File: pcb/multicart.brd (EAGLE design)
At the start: 55.5 x 86.4 mm, 14 parts, among them IC1 74HCT373N, IC2 M27C4001B, Q1 BS170

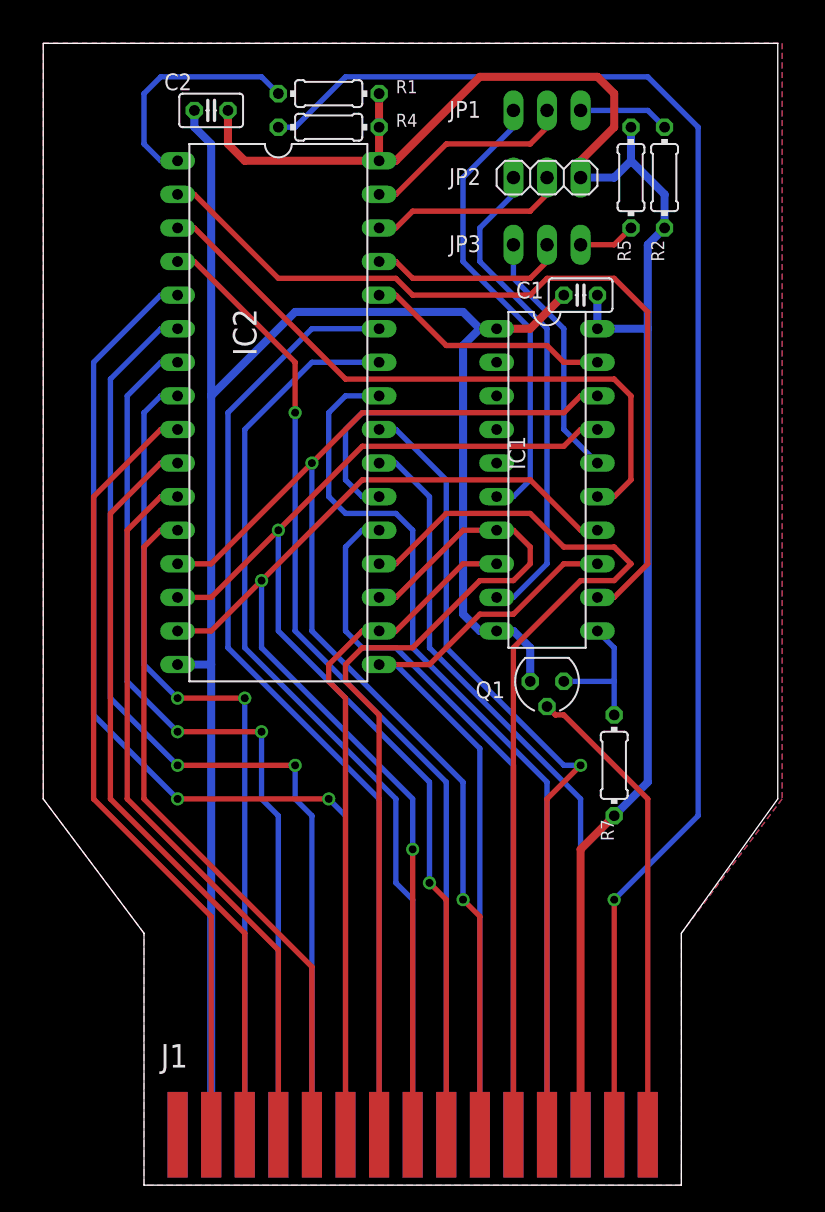
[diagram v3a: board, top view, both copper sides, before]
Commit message: Modified the design to support both 8k and 16k standard games.
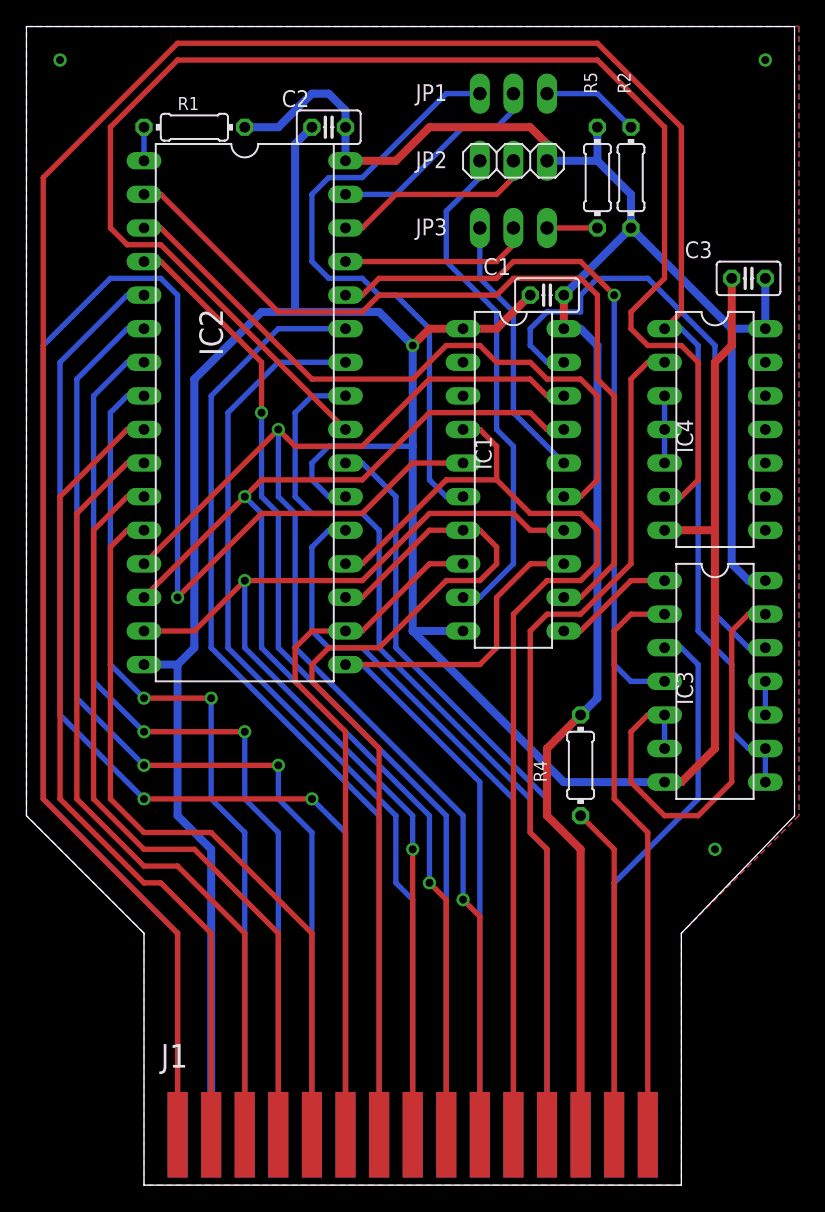
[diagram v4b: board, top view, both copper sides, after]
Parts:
- removed Q1: BS170, transistor-small-signal:SOT54E
- removed R7: 4k7, resistor:0204/7
- added C3: 100n, resistor:C025-025X050
- added IC3: 74HCT02N, 74xx-eu:DIL14
- added IC4: 74HCT00N, 74xx-eu:DIL14
- moved R4 51.9 mm to (47.0, 29.2), turned to 270 degrees
- moved R1 10.5 mm to (17.8, 77.5)
- moved C2 8.98 mm to (27.9, 77.5)
- moved JP1 2.84 mm to (41.9, 80.0)
- moved JP2 2.84 mm to (41.9, 74.9)
- moved JP3 2.84 mm to (41.9, 69.8)
- moved IC1 2.54 mm to (41.9, 50.8)
- moved R2 2.54 mm to (50.8, 73.7)
- moved C1 2.54 mm to (44.5, 64.8)
- moved IC2 2.54 mm to (21.6, 55.9)
- moved R5 2.54 mm to (48.3, 73.7)
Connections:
- new net N$14: IC4.3, IC4.4, IC4.5
- new net N$18: IC4.2, J1.12
- new net N$19: IC3.8, IC3.9, IC4.1, J1.1
- new net N$20: IC3.3, J1.R
- new net N$21: IC2.28, IC3.4
- new net N$22: IC1.5, J1.A
- new net N$23: IC3.13, IC3.5, IC3.6
- new net N$27: IC2.24, IC4.6
- net D6: now also IC1.4
- net GND: now also C3.2, IC3.7, IC4.7; no longer Q1.S
- net N$1: now also IC3.12; no longer IC2.28
- net N$17: now also IC3.10, IC3.11; no longer IC2.24, J1.12
- net N$7: now also IC3.1; no longer Q1.D, R7.1
- net N$8: now also IC3.2; no longer Q1.G
- net VCC: now also C3.1, IC3.14, IC4.14; no longer R7.2
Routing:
- net N$19: track 0.00 -> 186.4 mm
- net N$22: track 0.00 -> 125.3 mm, vias 0 -> 1
- net N$27: track 0.00 -> 112.2 mm
- net N$13: track 113.7 -> 25.2 mm, vias 1 -> 0
- net N$18: track 0.00 -> 65.4 mm
- net N$17: track 62.2 -> 2.54 mm, vias 1 -> 0
- net GND: track 158.5 -> 213.6 mm, vias 0 -> 1
- net N$21: track 0.00 -> 54.7 mm, vias 0 -> 1
- net N$20: track 0.00 -> 41.3 mm
- net N$23: track 0.00 -> 33.6 mm
- net N$1: track 18.6 -> 47.9 mm
- net VCC: track 138.5 -> 156.7 mm
- net N$9: track 18.1 -> 2.54 mm
- net N$6: track 34.7 -> 46.4 mm
- net D6: track 70.6 -> 78.7 mm
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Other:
- board size 55.5 x 86.4 mm -> 58.1 x 87.6 mm

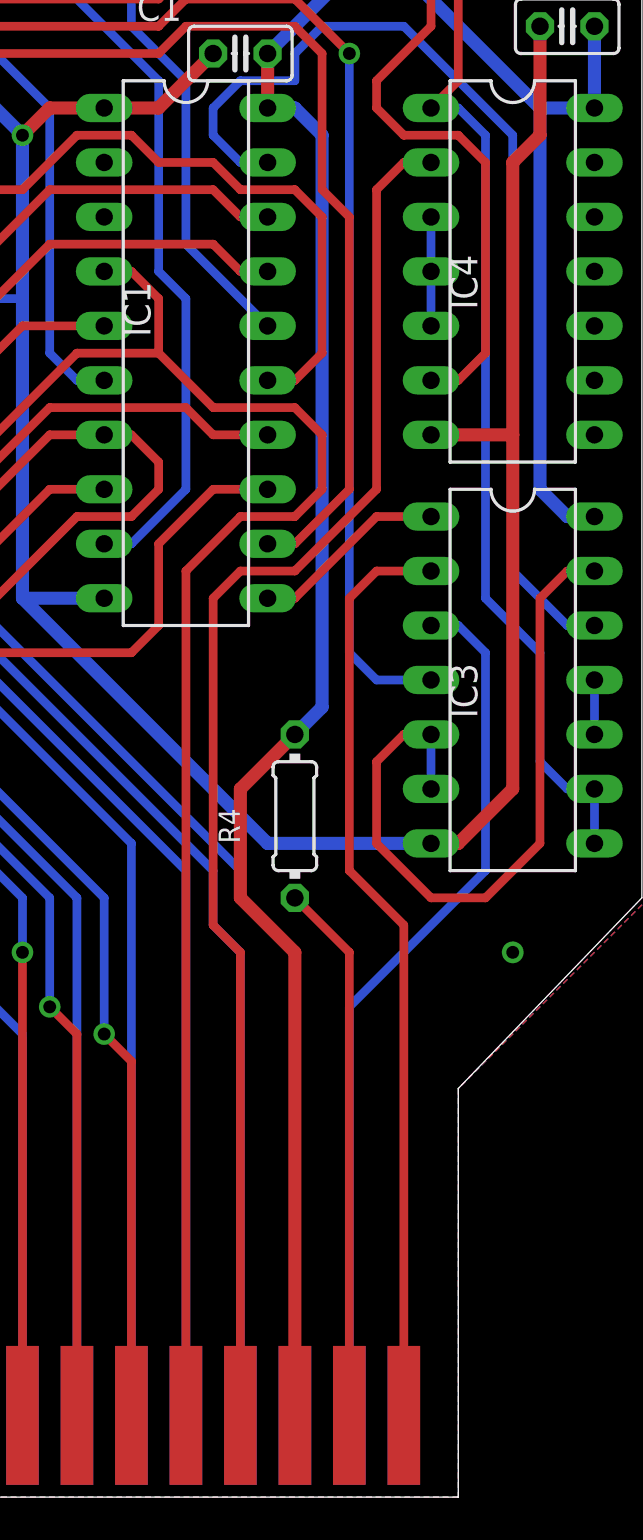
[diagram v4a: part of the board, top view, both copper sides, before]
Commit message: Removed the RD5 line resistor.
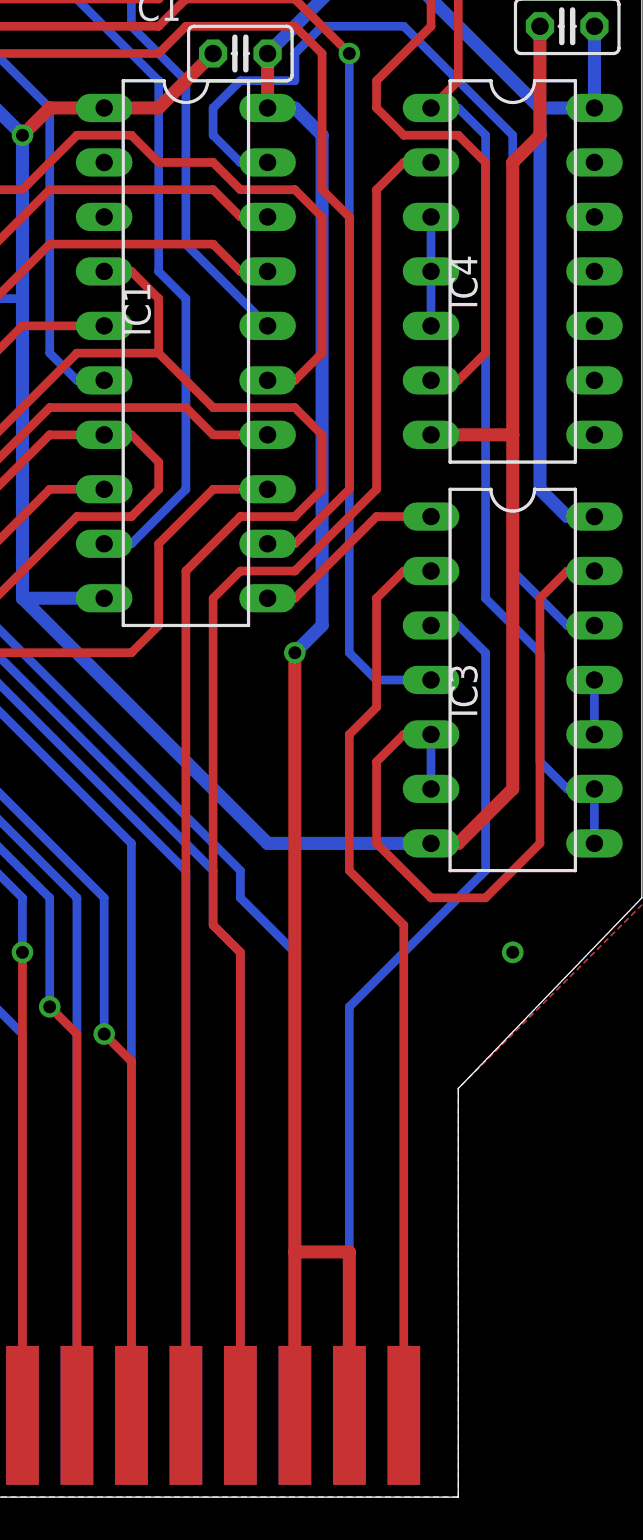
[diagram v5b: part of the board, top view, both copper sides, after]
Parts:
- removed R4: 4k7, resistor:0204/7
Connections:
- removed net N$13: J1.14, R4.2
- net VCC: now also J1.14; no longer R4.1
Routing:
- net N$13: track 25.2 -> 0.00 mm
- net VCC: track 156.7 -> 164.7 mm, vias 0 -> 1
- net N$8: track 43.5 -> 42.7 mm
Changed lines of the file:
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@@
 <attribute name="VALUE" x="50.6476" y="73.3044" size="0.9906" layer="27" ratio="10" rot="R90"/>
-</element>
-<element name="R4" library="resistor" package="0204/7" value="4k7" x="46.99" y="29.21" smashed="yes" rot="R270">
-<attribute name="NAME" x="44.4246" y="27.94" size="0.9906" layer="25" ratio="10" rot="R90"/>
-<attribute name="VALUE" x="46.2026" y="28.8544" size="0.9906" layer="27" ratio="10" rot="R90"/>
 </element>
 <element name="R5" library="resistor" package="0204/7" value="4k7" x="48.26" y="73.66" smashed="yes" rot="R90">
@@
 <contactref element="R2" pad="2"/>
 <contactref element="R5" pad="2"/>
-<wire x1="46.99" y1="22.86" x2="46.99" y2="1.27" width="0.6096" layer="1"/>
+<wire x1="46.99" y1="36.83" x2="46.99" y2="8.89" width="0.6096" layer="1"/>
+<wire x1="46.99" y1="8.89" x2="46.99" y2="1.27" width="0.6096" layer="1"/>
 <wire x1="50.8" y1="69.85" x2="50.8" y2="72.39" width="0.6096" layer="16"/>
 <wire x1="48.26" y1="77.47" x2="48.26" y2="74.93" width="0.6096" layer="16"/>
@@
 <contactref element="IC3" pad="14"/>
 <contactref element="IC4" pad="14"/>
-<contactref element="R4" pad="1"/>
-<wire x1="44.45" y1="30.48" x2="46.99" y2="33.02" width="0.6096" layer="1"/>
 <wire x1="60.96" y1="43.18" x2="59.69" y2="43.18" width="0.6096" layer="16"/>
 <wire x1="59.69" y1="43.18" x2="58.42" y2="44.45" width="0.6096" layer="16"/>
@@
 <wire x1="27.94" y1="80.01" x2="29.21" y2="78.74" width="0.6096" layer="16"/>
 <wire x1="29.21" y1="78.74" x2="29.21" y2="77.47" width="0.6096" layer="16"/>
-<wire x1="48.26" y1="34.29" x2="46.99" y2="33.02" width="0.6096" layer="16"/>
 <wire x1="58.42" y1="62.23" x2="50.8" y2="69.85" width="0.6096" layer="16"/>
 <wire x1="45.72" y1="64.77" x2="50.8" y2="69.85" width="0.6096" layer="16"/>
-<wire x1="46.99" y1="22.86" x2="44.45" y2="25.4" width="0.6096" layer="1"/>
-<wire x1="44.45" y1="25.4" x2="44.45" y2="30.48" width="0.6096" layer="1"/>
 <wire x1="29.21" y1="74.93" x2="33.02" y2="74.93" width="0.6096" layer="1"/>
 <wire x1="33.02" y1="74.93" x2="35.56" y2="77.47" width="0.6096" layer="1"/>
@@
 <wire x1="43.18" y1="77.47" x2="44.45" y2="76.2" width="0.6096" layer="1"/>
 <wire x1="44.45" y1="76.2" x2="44.45" y2="74.93" width="0.6096" layer="1"/>
-<wire x1="48.26" y1="34.29" x2="48.26" y2="60.96" width="0.6096" layer="16"/>
+<wire x1="45.72" y1="62.23" x2="45.72" y2="64.77" width="0.6096" layer="1"/>
+<contactref element="J1" pad="14"/>
+<wire x1="49.53" y1="1.27" x2="49.53" y2="8.89" width="0.6096" layer="1"/>
+<wire x1="49.53" y1="8.89" x2="46.99" y2="8.89" width="0.6096" layer="1"/>
+<via x="46.99" y="36.83" extent="1-16" drill="0.6" shape="octagon"/>
+<wire x1="46.99" y1="36.83" x2="48.26" y2="38.1" width="0.6096" layer="16"/>
+<wire x1="48.26" y1="38.1" x2="48.26" y2="60.96" width="0.6096" layer="16"/>
 <wire x1="48.26" y1="60.96" x2="46.99" y2="62.23" width="0.6096" layer="16"/>
 <wire x1="46.99" y1="62.23" x2="45.72" y2="62.23" width="0.6096" layer="16"/>
-<wire x1="45.72" y1="62.23" x2="45.72" y2="64.77" width="0.6096" layer="1"/>
 </signal>
 <signal name="GND">
@@
 <contactref element="J1" pad="15"/>
 <contactref element="IC3" pad="2"/>
-<wire x1="49.53" y1="39.37" x2="50.8" y2="40.64" width="0.4064" layer="1"/>
-<wire x1="50.8" y1="40.64" x2="53.34" y2="40.64" width="0.4064" layer="1"/>
 <wire x1="52.07" y1="1.27" x2="52.07" y2="24.13" width="0.4064" layer="1"/>
 <wire x1="52.07" y1="24.13" x2="49.53" y2="26.67" width="0.4064" layer="1"/>
-<wire x1="49.53" y1="26.67" x2="49.53" y2="39.37" width="0.4064" layer="1"/>
+<wire x1="53.34" y1="40.64" x2="52.07" y2="40.64" width="0.4064" layer="1"/>
+<wire x1="52.07" y1="40.64" x2="50.8" y2="39.37" width="0.4064" layer="1"/>
+<wire x1="50.8" y1="39.37" x2="50.8" y2="34.29" width="0.4064" layer="1"/>
+<wire x1="50.8" y1="34.29" x2="49.53" y2="33.02" width="0.4064" layer="1"/>
+<wire x1="49.53" y1="33.02" x2="49.53" y2="26.67" width="0.4064" layer="1"/>
 </signal>
 <signal name="N$21">
@@
 <wire x1="55.88" y1="26.67" x2="49.53" y2="20.32" width="0.4064" layer="16"/>
 </signal>
-<signal name="N$13">
-<contactref element="J1" pad="14"/>
-<contactref element="R4" pad="2"/>
-<wire x1="49.53" y1="1.27" x2="49.53" y2="22.86" width="0.4064" layer="1"/>
-<wire x1="49.53" y1="22.86" x2="46.99" y2="25.4" width="0.4064" layer="1"/>
-</signal>
 <signal name="N$17">

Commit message: Optimized the design a little.
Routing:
- net N$6: track 46.4 -> 34.6 mm
- net N$10: track 16.6 -> 21.7 mm
- net N$5: track 38.5 -> 37.4 mm
- net N$2: track 20.4 -> 21.2 mm
- net N$8: track 42.7 -> 43.5 mm
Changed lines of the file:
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@@
 <wire x1="40.64" y1="64.77" x2="31.75" y2="64.77" width="0.4064" layer="1"/>
 <wire x1="41.91" y1="66.04" x2="46.99" y2="66.04" width="0.4064" layer="1"/>
-<wire x1="49.53" y1="44.45" x2="49.53" y2="57.15" width="0.4064" layer="1"/>
-<wire x1="49.53" y1="57.15" x2="48.26" y2="58.42" width="0.4064" layer="1"/>
-<wire x1="48.26" y1="58.42" x2="48.26" y2="64.77" width="0.4064" layer="1"/>
+<wire x1="49.53" y1="44.45" x2="49.53" y2="62.23" width="0.4064" layer="1"/>
 <wire x1="48.26" y1="64.77" x2="46.99" y2="66.04" width="0.4064" layer="1"/>
+<wire x1="49.53" y1="62.23" x2="48.26" y2="63.5" width="0.4064" layer="1"/>
+<wire x1="48.26" y1="63.5" x2="48.26" y2="64.77" width="0.4064" layer="1"/>
 </signal>
 <signal name="D0">
@@
 <contactref element="C3" pad="2"/>
 <wire x1="25.4" y1="63.5" x2="31.75" y2="63.5" width="0.6096" layer="16"/>
-<wire x1="58.42" y1="66.04" x2="58.42" y2="60.96" width="0.6096" layer="1"/>
 <wire x1="45.72" y1="27.94" x2="53.34" y2="27.94" width="0.6096" layer="16"/>
 <wire x1="54.61" y1="27.94" x2="53.34" y2="27.94" width="0.6096" layer="1"/>
@@
 <wire x1="16.51" y1="36.83" x2="17.78" y2="38.1" width="0.6096" layer="16"/>
 <wire x1="17.78" y1="38.1" x2="17.78" y2="58.42" width="0.6096" layer="16"/>
-<wire x1="58.42" y1="60.96" x2="57.15" y2="59.69" width="0.6096" layer="1"/>
-<wire x1="57.15" y1="59.69" x2="57.15" y2="46.99" width="0.6096" layer="1"/>
+<wire x1="57.15" y1="64.77" x2="57.15" y2="46.99" width="0.6096" layer="1"/>
 <wire x1="57.15" y1="46.99" x2="57.15" y2="30.48" width="0.6096" layer="1"/>
 <wire x1="19.05" y1="1.27" x2="19.05" y2="22.86" width="0.6096" layer="16"/>
@@
 <wire x1="34.29" y1="39.37" x2="45.72" y2="27.94" width="0.6096" layer="16"/>
 <wire x1="38.1" y1="39.37" x2="34.29" y2="39.37" width="0.6096" layer="16"/>
+<wire x1="57.15" y1="64.77" x2="58.42" y2="66.04" width="0.6096" layer="1"/>
 </signal>
 <signal name="N$9">
@@
 <wire x1="39.37" y1="73.66" x2="36.83" y2="71.12" width="0.4064" layer="16"/>
 <wire x1="36.83" y1="71.12" x2="36.83" y2="67.31" width="0.4064" layer="16"/>
-<wire x1="41.91" y1="44.45" x2="39.37" y2="41.91" width="0.4064" layer="16"/>
+<wire x1="40.64" y1="43.18" x2="39.37" y2="41.91" width="0.4064" layer="16"/>
 <wire x1="39.37" y1="41.91" x2="38.1" y2="41.91" width="0.4064" layer="16"/>
-<wire x1="40.64" y1="54.61" x2="40.64" y2="63.5" width="0.4064" layer="16"/>
 <wire x1="40.64" y1="63.5" x2="36.83" y2="67.31" width="0.4064" layer="16"/>
-<wire x1="40.64" y1="54.61" x2="41.91" y2="53.34" width="0.4064" layer="16"/>
-<wire x1="41.91" y1="53.34" x2="41.91" y2="44.45" width="0.4064" layer="16"/>
+<wire x1="40.64" y1="63.5" x2="40.64" y2="43.18" width="0.4064" layer="16"/>
 </signal>
 <signal name="N$12">
@@
 <contactref element="IC1" pad="6"/>
 <contactref element="JP1" pad="3"/>
-<wire x1="39.37" y1="80.01" x2="36.83" y2="80.01" width="0.4064" layer="16"/>
-<wire x1="36.83" y1="80.01" x2="30.48" y2="73.66" width="0.4064" layer="16"/>
-<wire x1="30.48" y1="73.66" x2="27.94" y2="73.66" width="0.4064" layer="16"/>
-<wire x1="27.94" y1="73.66" x2="26.67" y2="72.39" width="0.4064" layer="16"/>
-<wire x1="26.67" y1="72.39" x2="26.67" y2="67.31" width="0.4064" layer="16"/>
-<wire x1="26.67" y1="67.31" x2="27.94" y2="66.04" width="0.4064" layer="16"/>
-<wire x1="27.94" y1="66.04" x2="30.48" y2="66.04" width="0.4064" layer="16"/>
-<wire x1="30.48" y1="66.04" x2="31.75" y2="64.77" width="0.4064" layer="16"/>
+<wire x1="39.37" y1="80.01" x2="38.1" y2="80.01" width="0.4064" layer="16"/>
+<wire x1="38.1" y1="80.01" x2="36.83" y2="80.01" width="0" layer="19" extent="1-16"/>
 <wire x1="38.1" y1="49.53" x2="36.83" y2="49.53" width="0.4064" layer="16"/>
 <wire x1="36.83" y1="49.53" x2="35.56" y2="50.8" width="0.4064" layer="16"/>
-<wire x1="35.56" y1="50.8" x2="35.56" y2="62.23" width="0.4064" layer="16"/>
-<wire x1="35.56" y1="62.23" x2="33.02" y2="64.77" width="0.4064" layer="16"/>
-<wire x1="33.02" y1="64.77" x2="31.75" y2="64.77" width="0.4064" layer="16"/>
+<wire x1="35.56" y1="50.8" x2="35.56" y2="77.47" width="0.4064" layer="16"/>
+<wire x1="35.56" y1="77.47" x2="38.1" y2="80.01" width="0.4064" layer="16"/>
 </signal>
 <signal name="N$10">
 <contactref element="IC2" pad="31"/>
 <contactref element="JP1" pad="2"/>
-<wire x1="29.21" y1="72.39" x2="33.02" y2="72.39" width="0.4064" layer="16"/>
-<wire x1="33.02" y1="72.39" x2="38.1" y2="77.47" width="0.4064" layer="16"/>
-<wire x1="38.1" y1="77.47" x2="40.64" y2="77.47" width="0.4064" layer="16"/>
-<wire x1="40.64" y1="77.47" x2="41.91" y2="78.74" width="0.4064" layer="16"/>
-<wire x1="41.91" y1="78.74" x2="41.91" y2="80.01" width="0.4064" layer="16"/>
+<wire x1="41.91" y1="80.01" x2="41.91" y2="81.28" width="0.4064" layer="16"/>
+<wire x1="41.91" y1="81.28" x2="40.64" y2="82.55" width="0.4064" layer="16"/>
+<wire x1="40.64" y1="82.55" x2="38.1" y2="82.55" width="0.4064" layer="16"/>
+<wire x1="38.1" y1="82.55" x2="34.29" y2="78.74" width="0.4064" layer="16"/>
+<wire x1="34.29" y1="78.74" x2="34.29" y2="73.66" width="0.4064" layer="16"/>
+<wire x1="34.29" y1="73.66" x2="33.02" y2="72.39" width="0.4064" layer="16"/>
+<wire x1="33.02" y1="72.39" x2="29.21" y2="72.39" width="0.4064" layer="16"/>
 </signal>
 <signal name="N$11">
@@
 <contactref element="IC1" pad="16"/>
 <contactref element="JP3" pad="3"/>
-<wire x1="41.91" y1="55.88" x2="45.72" y2="52.07" width="0.4064" layer="16"/>
 <wire x1="39.37" y1="69.85" x2="39.37" y2="66.04" width="0.4064" layer="16"/>
-<wire x1="41.91" y1="55.88" x2="41.91" y2="63.5" width="0.4064" layer="16"/>
 <wire x1="41.91" y1="63.5" x2="39.37" y2="66.04" width="0.4064" layer="16"/>
+<wire x1="45.72" y1="52.07" x2="44.45" y2="52.07" width="0.4064" layer="16"/>
+<wire x1="44.45" y1="52.07" x2="41.91" y2="54.61" width="0.4064" layer="16"/>
+<wire x1="41.91" y1="54.61" x2="41.91" y2="63.5" width="0.4064" layer="16"/>
 </signal>
 <signal name="N$15">
@@
 <wire x1="52.07" y1="1.27" x2="52.07" y2="24.13" width="0.4064" layer="1"/>
 <wire x1="52.07" y1="24.13" x2="49.53" y2="26.67" width="0.4064" layer="1"/>
-<wire x1="53.34" y1="40.64" x2="52.07" y2="40.64" width="0.4064" layer="1"/>
-<wire x1="52.07" y1="40.64" x2="50.8" y2="39.37" width="0.4064" layer="1"/>
-<wire x1="50.8" y1="39.37" x2="50.8" y2="34.29" width="0.4064" layer="1"/>
-<wire x1="50.8" y1="34.29" x2="49.53" y2="33.02" width="0.4064" layer="1"/>
-<wire x1="49.53" y1="33.02" x2="49.53" y2="26.67" width="0.4064" layer="1"/>
+<wire x1="49.53" y1="26.67" x2="49.53" y2="39.37" width="0.4064" layer="1"/>
+<wire x1="49.53" y1="39.37" x2="50.8" y2="40.64" width="0.4064" layer="1"/>
+<wire x1="50.8" y1="40.64" x2="53.34" y2="40.64" width="0.4064" layer="1"/>
 </signal>
 <signal name="N$21">
